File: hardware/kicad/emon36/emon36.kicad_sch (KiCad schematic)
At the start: 2 parts, among them U1 ESP32-C3-WROOM-02-N4

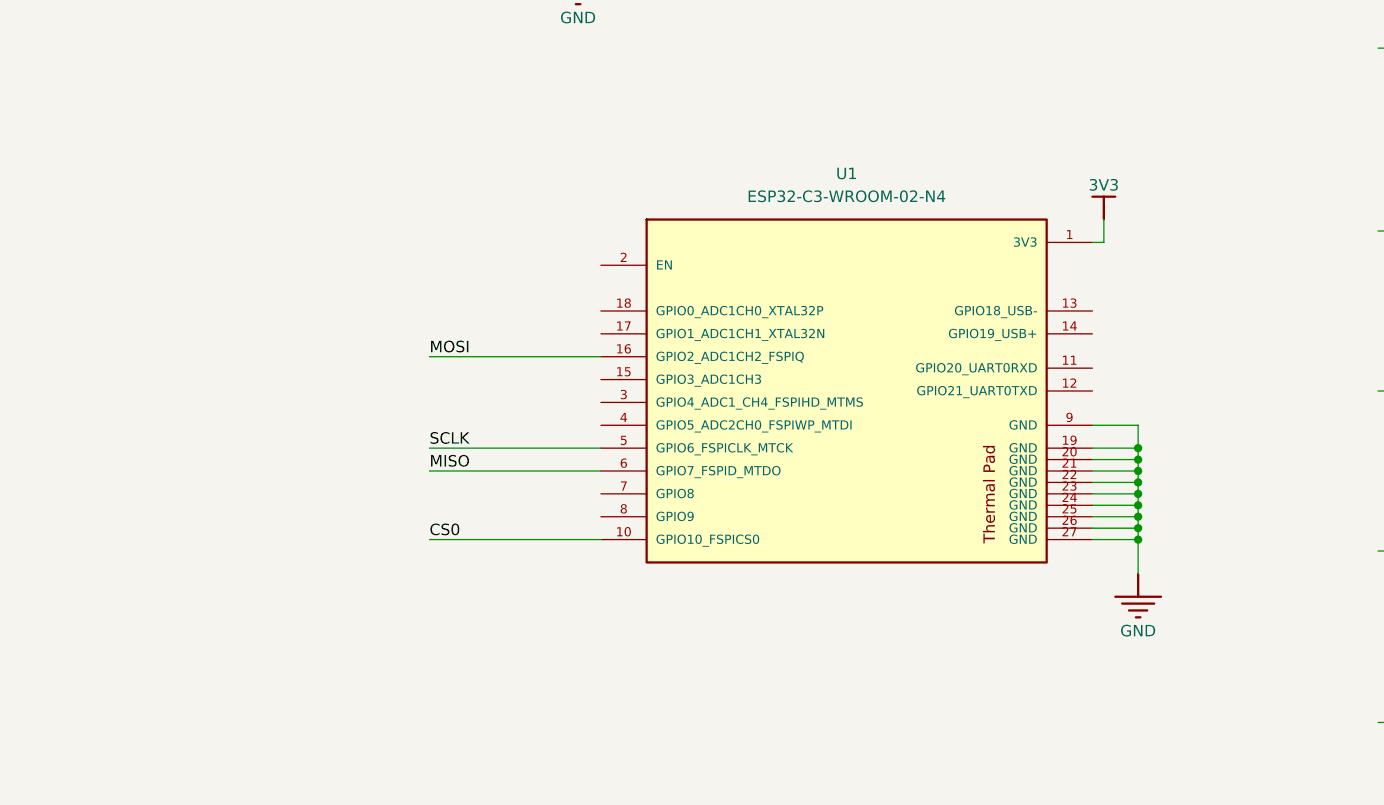
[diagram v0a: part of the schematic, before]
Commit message: Add preliminary USB interface
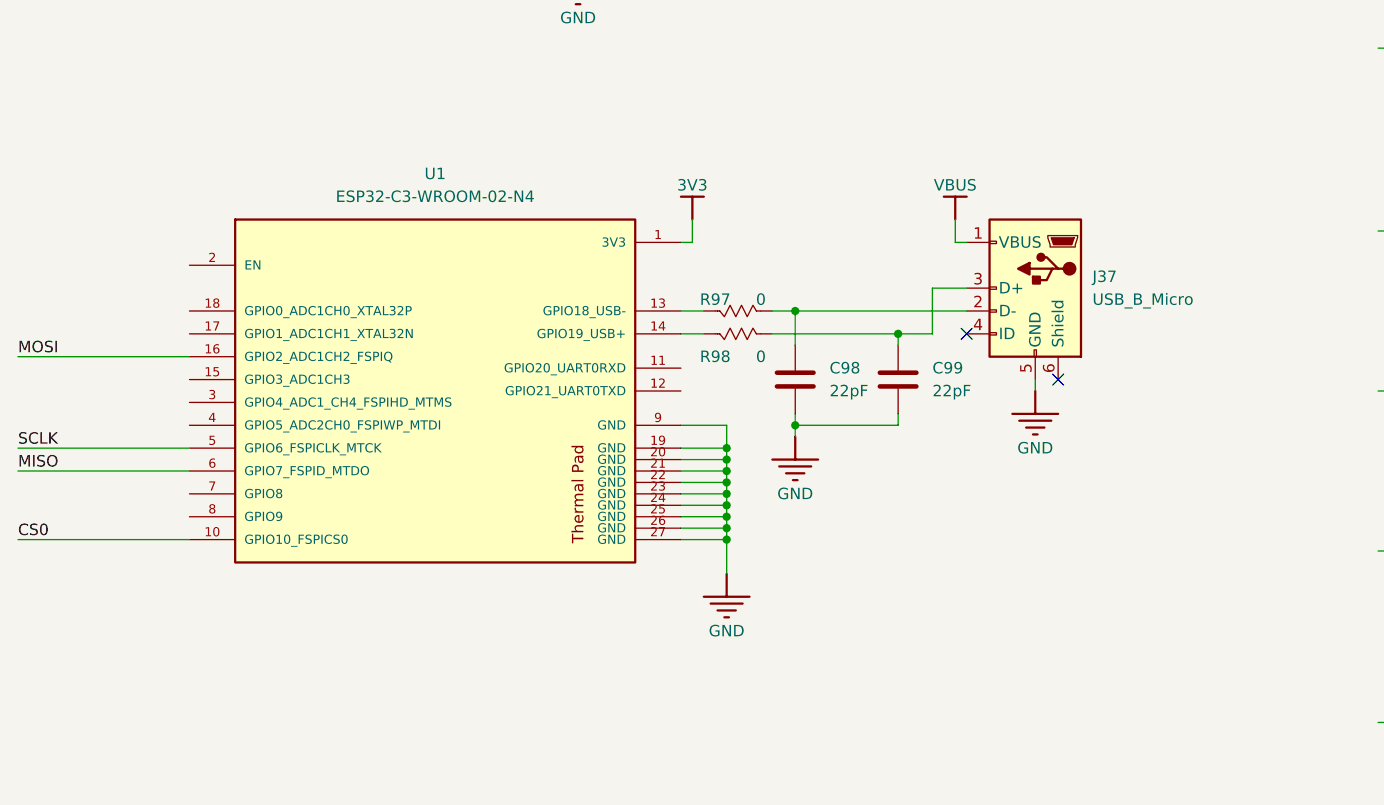
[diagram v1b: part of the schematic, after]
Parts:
- added C98, C99: 22pF, Capacitor_SMD:C_0603_1608Metric, symbol Device:C
- added J37: USB_B_Micro, Connector_USB:USB_Micro-B_Wuerth_629105150521, symbol Connector:USB_B_Micro
- added R97, R98: 0, Resistor_SMD:R_0603_1608Metric, symbol emon36:R_US
- C1: footprint CAPC2013X145X48ML20T23 -> emon36:CAPC2013X145X48ML20T23
- U1: footprint MODULE_ESP32-C3-WROOM-02-H4 -> emon36:MODULE_ESP32-C3-WROOM-02-H4
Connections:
- net 3V3: now also J37.1 (VBUS)
- net GND: now also C98.2, C99.2, J37.5 (GND)
- net at U1.13 (GPIO18_USB-): now also R97.2
- net at U1.14 (GPIO19_USB+): now also R98.2
- new net: C99.1, J37.3 (D+), R98.1
- new net: C98.1, J37.2 (D-), R97.1
- no-connect marks 0 -> 2
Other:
- moved on the sheet: U1

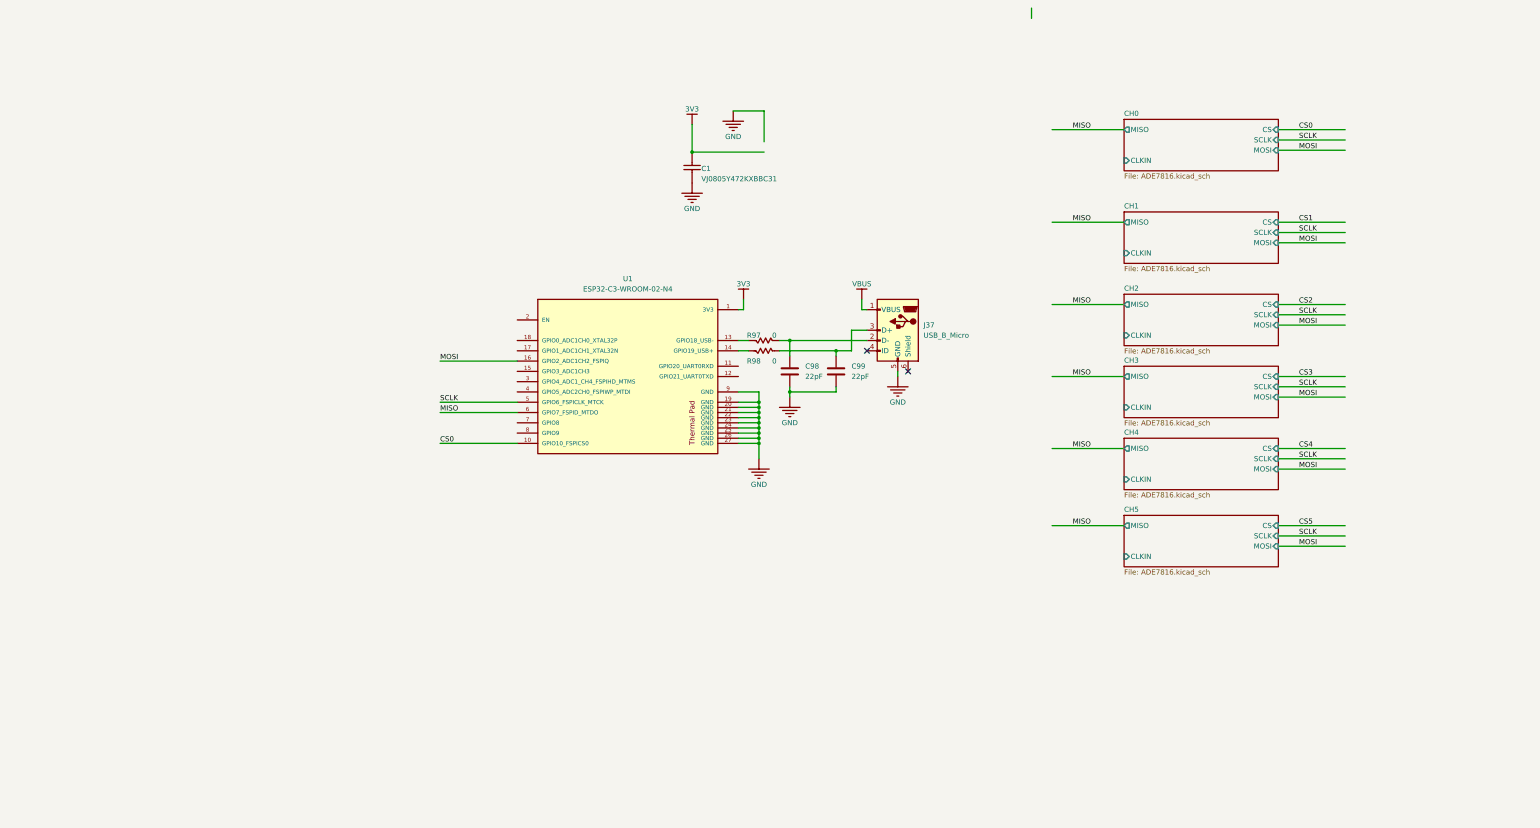
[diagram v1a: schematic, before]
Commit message: Reverted to stacked 3.5mm connectors. Now has 42 channels. Added OLED, switches, power system. Cleaned up channel page.
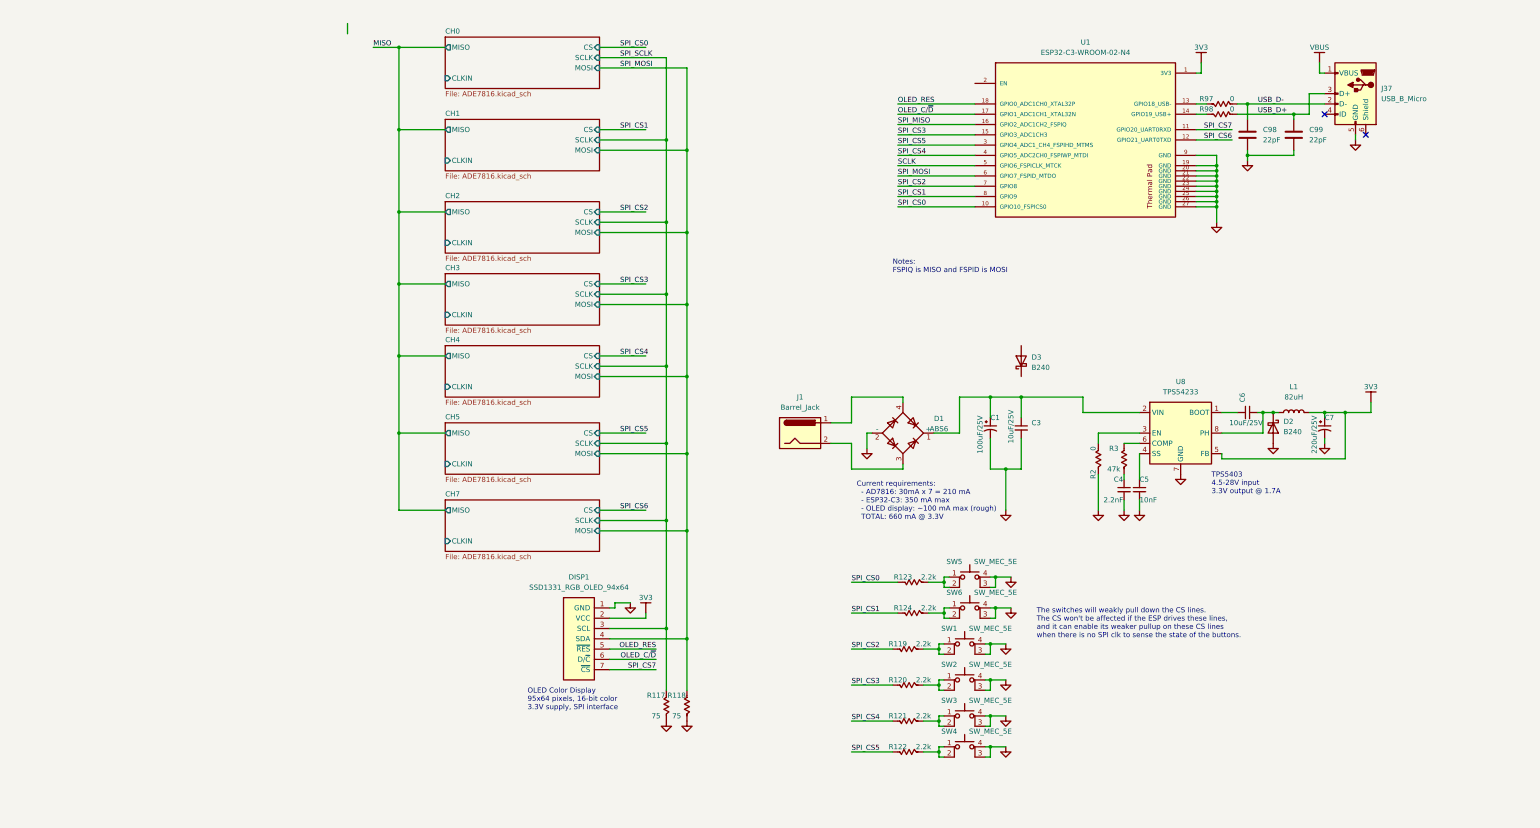
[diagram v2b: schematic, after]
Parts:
- removed C1: VJ0805Y472KXBBC31, emon36:CAPC2013X145X48ML20T23, symbol Top-altium-import:1_CAP
- added C1: 100uF/25V, Capacitor_Tantalum_SMD:CP_EIA-1608-08_AVX-J, symbol Device:C_Polarized_Small_US
- added C3, C6: 10uF/25V, Capacitor_SMD:C_0603_1608Metric, symbol Device:C_Small
- added C4: 2.2nF, Capacitor_SMD:C_0603_1608Metric, symbol Device:C_Small
- added C5: 10nF, Capacitor_SMD:C_0603_1608Metric, symbol Device:C_Small
- added C7: 220uF/25V, Capacitor_Tantalum_SMD:CP_EIA-1608-08_AVX-J, symbol Device:C_Polarized_Small_US
- added D1: ABS6, Diode_SMD:Diode_Bridge_Diotec_ABS, symbol Diode_Bridge:ABS6
- added D2, D3: B240, Diode_SMD:D_SMB, symbol Diode:B240
- added DISP1: SSD1331_RGB_OLED_94x64, emon36:SSD1331_RGB_OLED_96x64, symbol emon36:SSD1331_RGB_OLED_94x64
- added J1: Barrel_Jack, Connector_BarrelJack:BarrelJack_SwitchcraftConxall_RAPC10U_Horizontal, symbol Connector:Barrel_Jack
- added L1: 82uH, Inductor_THT:L_Radial_D7.5mm_P3.50mm_Fastron_07P, symbol Device:L
- added R117, R118: 75, Resistor_SMD:R_0603_1608Metric, symbol emon36:R_US
- added R119, R120, R121, R122, R123, R124: 2.2k, Resistor_SMD:R_0603_1608Metric, symbol emon36:R_US
- added R2: 0, Resistor_SMD:R_0603_1608Metric, symbol emon36:R_US
- added R3: 47k, Resistor_SMD:R_0603_1608Metric, symbol emon36:R_US
- added SW1, SW2, SW3, SW4, SW5, SW6: SW_MEC_5E, Button_Switch_SMD:SW_Push_1P1T_NO_6x6mm_H13mm, symbol Switch:SW_MEC_5E
- added U8: TPS54233, Package_SO:SOIC-8_3.9x4.9mm_P1.27mm, symbol Regulator_Switching:TPS54233
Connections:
- net 3V3: now also C7.1, DISP1.2 (VCC), L1.2, U8.5 (FB)
- net GND: now also C1.2, C3.2, C4.2, C5.2, C7.2, D1.2 (-), D2.2 (A), DISP1.1 (GND), R117.2, R118.2, R2.2, SW1.3 (K), SW1.4 (A), SW2.3 (K), SW2.4 (A), SW3.3 (K), SW3.4 (A), SW4.3 (K), SW4.4 (A), SW5.3 (K), SW5.4 (A), SW6.3 (K), SW6.4 (A), U8.7 (GND)
- net MISO: no longer U1.6 (GPIO7_FSPID_MTDO)
- net USB_D+: now reaches C99.1, J37.3 (D+), R98.1
- net USB_D-: now reaches C98.1, J37.2 (D-), R97.1
- net SPI_CS7: now reaches U1.11 (GPIO20_UART0RXD)
- net SPI_CS7: now also DISP1.7 (~{CS})
- net SPI_CS6: now reaches U1.12 (GPIO21_UART0TXD)
- net SPI_CS3: now reaches U1.15 (GPIO3_ADC1CH3)
- net SPI_CS3: now also R120.1
- net OLED_C/~{D}: now reaches U1.17 (GPIO1_ADC1CH1_XTAL32N)
- net OLED_C/~{D}: now also DISP1.6 (D/~{C})
- net OLED_RES: now reaches U1.18 (GPIO0_ADC1CH0_XTAL32P)
- net OLED_RES: now also DISP1.5 (~{RES})
- net SPI_CS5: now reaches U1.3 (GPIO4_ADC1_CH4_FSPIHD_MTMS)
- net SPI_CS5: now also R122.1
- net SPI_CS4: now reaches U1.4 (GPIO5_ADC2CH0_FSPIWP_MTDI)
- net SPI_CS4: now also R121.1
- net SPI_CS2: now reaches U1.7 (GPIO8)
- net SPI_CS2: now also R119.1
- net SPI_CS1: now reaches U1.8 (GPIO9)
- net SPI_CS1: now also R124.1
- net CS0 renamed SPI_CS0
- net SPI_CS0: now also R123.1
- net MOSI renamed SPI_MISO
- new net: R120.2, SW2.1, SW2.2
- new net: R122.2, SW4.1, SW4.2
- new net: R124.2, SW6.1, SW6.2
- new net: C1.1, C3.1, D1.1 (+), U8.2 (VIN)
- new net: C6.1, U8.1 (BOOT)
- new net: R2.1, U8.3 (EN)
- new net: C5.1, U8.4 (SS)
- new net: R3.1, U8.6 (COMP)
- new net: C6.2, D2.1 (K), L1.1, U8.8 (PH)
- new net: D1.4, J1.1
- new net: D1.3, J1.2
- new net: R121.2, SW3.1, SW3.2
- new net: C4.1, R3.2
- new net: R123.2, SW5.1, SW5.2
- new net: R119.2, SW1.1, SW1.2
- new net SPI_MOSI: DISP1.4 (SDA), R118.1, U1.6 (GPIO7_FSPID_MTDO)
- new net SPI_SCLK: DISP1.3 (SCL), R117.1
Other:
- added sheet CH7 (ADE7816.kicad_sch)
- note added: "Current requirements: - AD7816: 30mA x 7 = 210 mA - ESP32-C3: 350 mA max - OLED display: ~100 mA max (rough) TOTAL: 660 mA @ 3.3V"
- note added: "Notes: FSPIQ is MISO and FSPID is MOSI"
- note added: "OLED Color Display 95x64 pixels, 16-bit color 3.3V supply, SPI interface"
- note added: "TPS5403 4.5-28V input 3.3V output @ 1.7A"
- note added: "The switches will weakly pull down the CS lines. The CS won't be affected if the ESP drives these lines, and it can enable its weaker pullup on these CS lines when there is no SPI clk to sense the state of the buttons."
- moved on the sheet: C98, C99, J37, R97, R98, U1

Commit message: schematics: Added todo list, 2nd AC connector, series caps to SPI terminations.
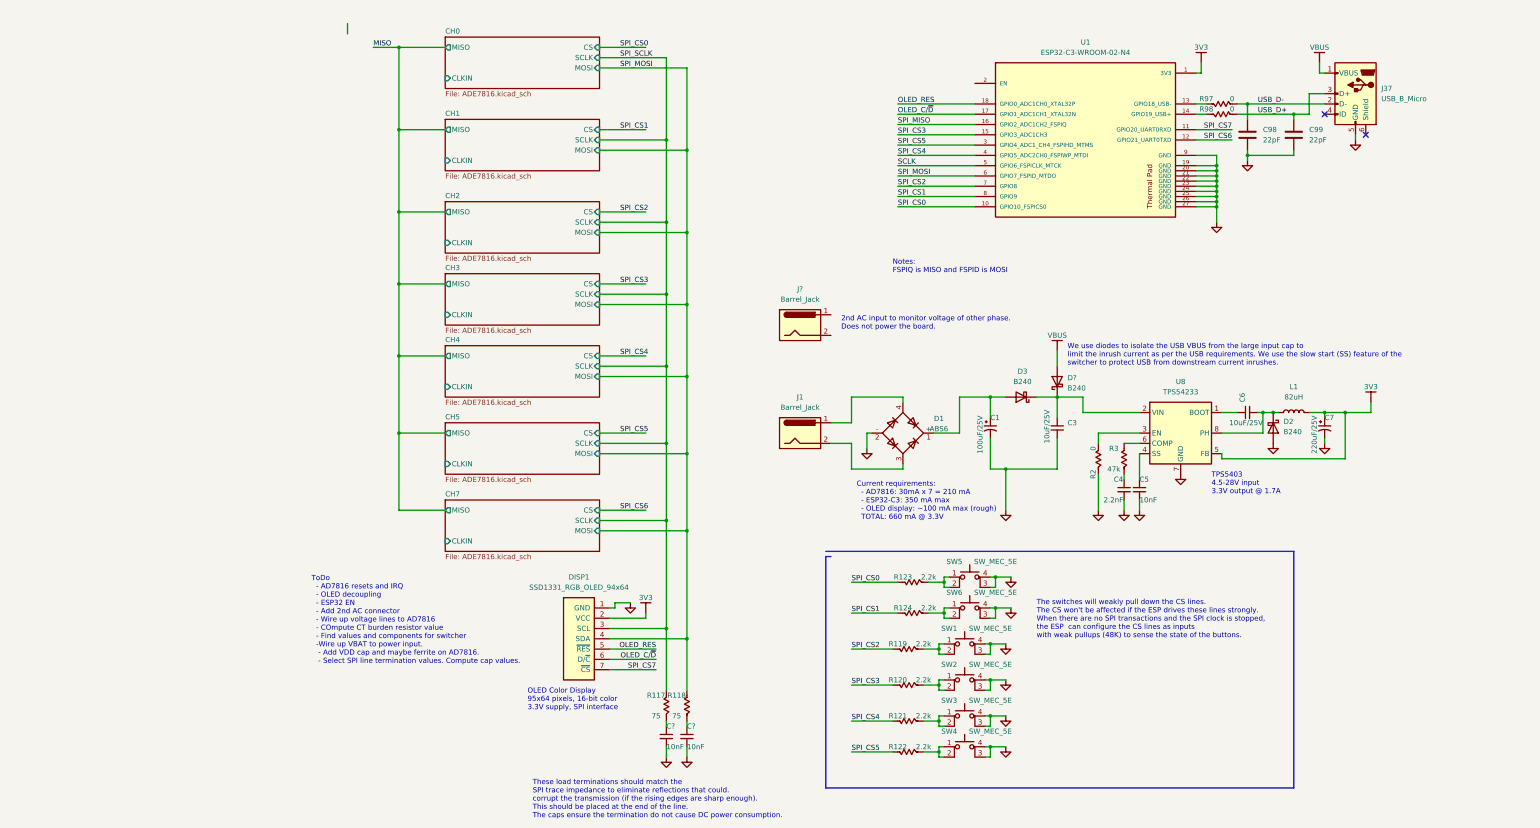
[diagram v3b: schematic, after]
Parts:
- added C? (x2): 10nF, Capacitor_SMD:C_0603_1608Metric, symbol Device:C_Small
- added D?: B240, Diode_SMD:D_SMB, symbol Diode:B240
- added J?: Barrel_Jack, Connector_BarrelJack:BarrelJack_SwitchcraftConxall_RAPC10U_Horizontal, symbol Connector:Barrel_Jack
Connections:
- net 3V3: now also D?.2 (A)
- net GND: now also C?.2, C?.2; no longer R117.2, R118.2
- net at C3.1, U8.2 (VIN): now also D3.1 (K), D?.1 (K); no longer C1.1, D1.1 (+)
- net at D3.2 (A): now also C1.1, D1.1 (+)
- new net: C?.1, R118.2
- new net: C?.1, R117.2
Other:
- note added: "2nd AC input to monitor voltage of other phase. Does not power the board."
- note added: "The switches will weakly pull down the CS lines. The CS won't be affected if the ESP drives these lines strongly. When there are no SPI transactions and the SPI clock is stopped, the ESP can configure the CS lines as inputs with weak pullups (48K) to sense the state of the buttons."
- note added: "These load terminations should match the SPI trace impedance to eliminate reflections that could. corrupt the transmission (if the rising edges are sharp enough). This should be placed at the end of the line. The caps ensure the termination do not cause DC power consumption."
- note added: "ToDo - AD7816 resets and IRQ - OLED decoupling - ESP32 EN - Add 2nd AC connector - Wire up voltage lines to AD7816 - COmpute CT burden resistor value - Find values and components for switcher -Wire up VBAT to power input. - Add VDD cap and maybe ferrite on AD7816. - Select SPI line termination values. Compute cap values."
- note added: "We use diodes to isolate the USB VBUS from the large input cap to limit the inrush current as per the USB requirements. We use the slow start (SS) feature of the switcher to protect USB from downstream current inrushes."
- note removed: "The switches will weakly pull down the CS lines. The CS won't be affected if the ESP drives these lines, and it can enable its weaker pullup on these CS lines when there is no SPI clk to sense the state of the buttons."
- moved on the sheet: C3, D3
